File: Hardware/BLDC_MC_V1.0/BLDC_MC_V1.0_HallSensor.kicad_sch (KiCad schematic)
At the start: 21 parts, among them J5 Conn_02x03_Counter_Clockwise, U10 TLV9061IDBVR, U11 TLV9061IDBVR, U3 TLV9061IDBVR

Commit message: Add voltage sensor to measure the 3 phase voltage of inverter bridge
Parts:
- R15, R49, R52: LCSC_PN C98220 -> C95204; MP RC0603FR-0710KL -> RT0603BRD0710KL
- R46, R48, R51: LCSC_PN C100001 -> C723585; MP RC0603FR-0730KL -> RT0603BRD0730KL

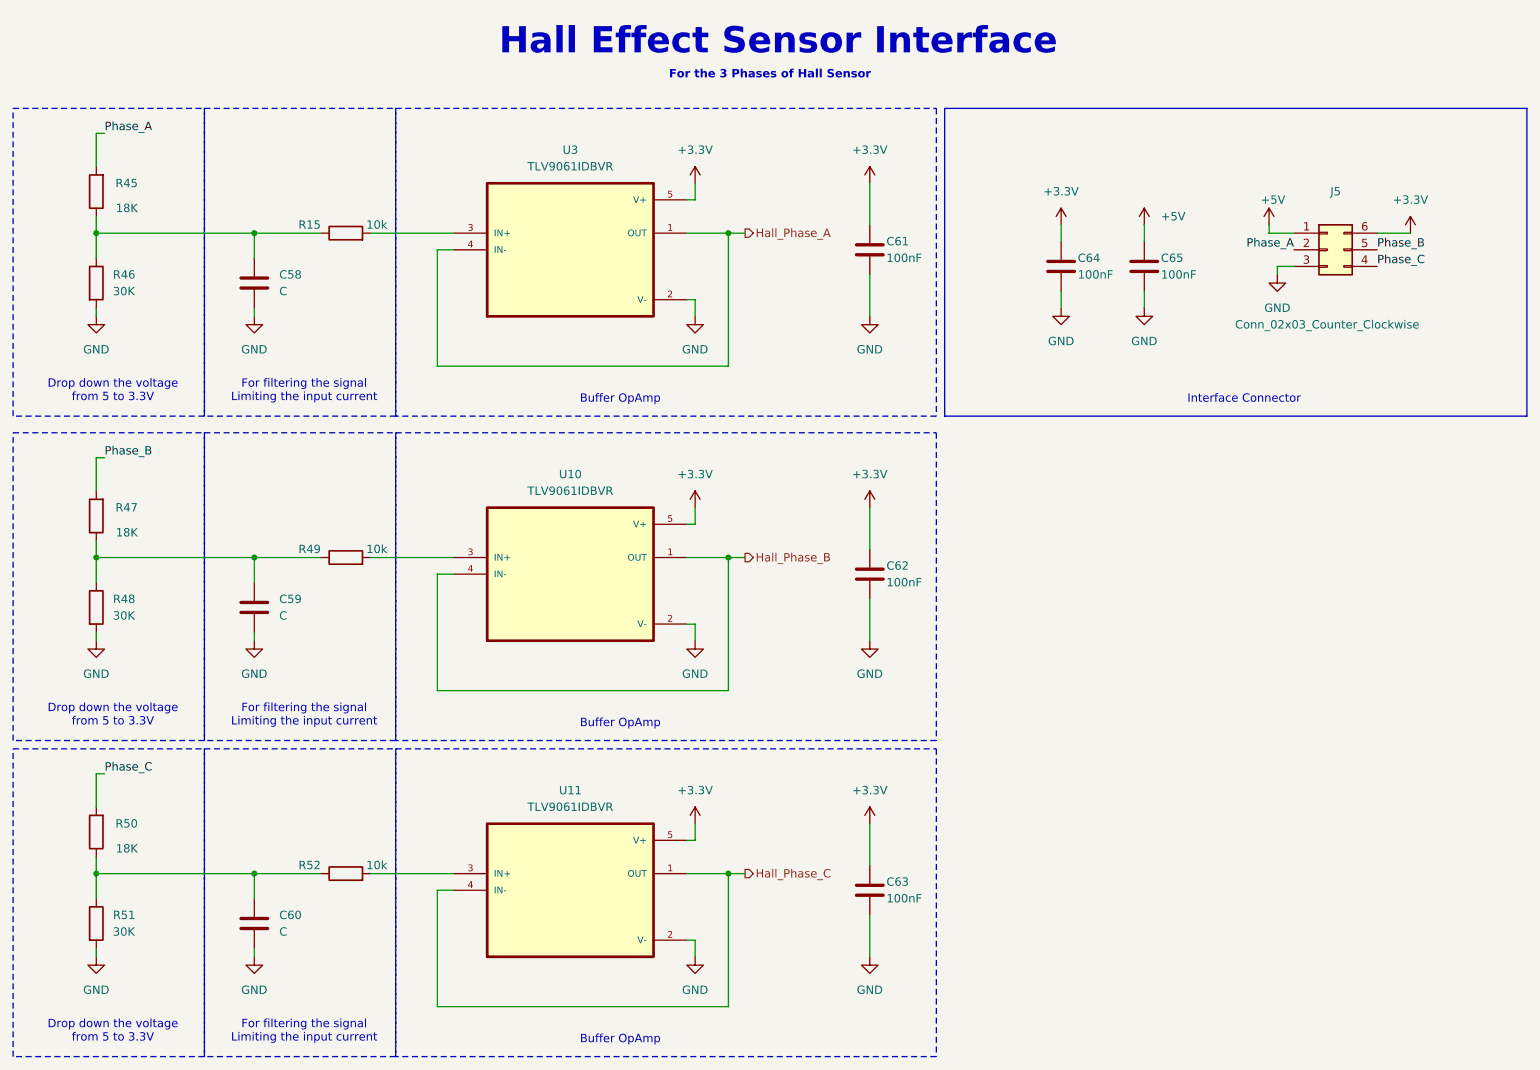
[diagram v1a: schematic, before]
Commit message: Add bypass capacitors for the OpAmps
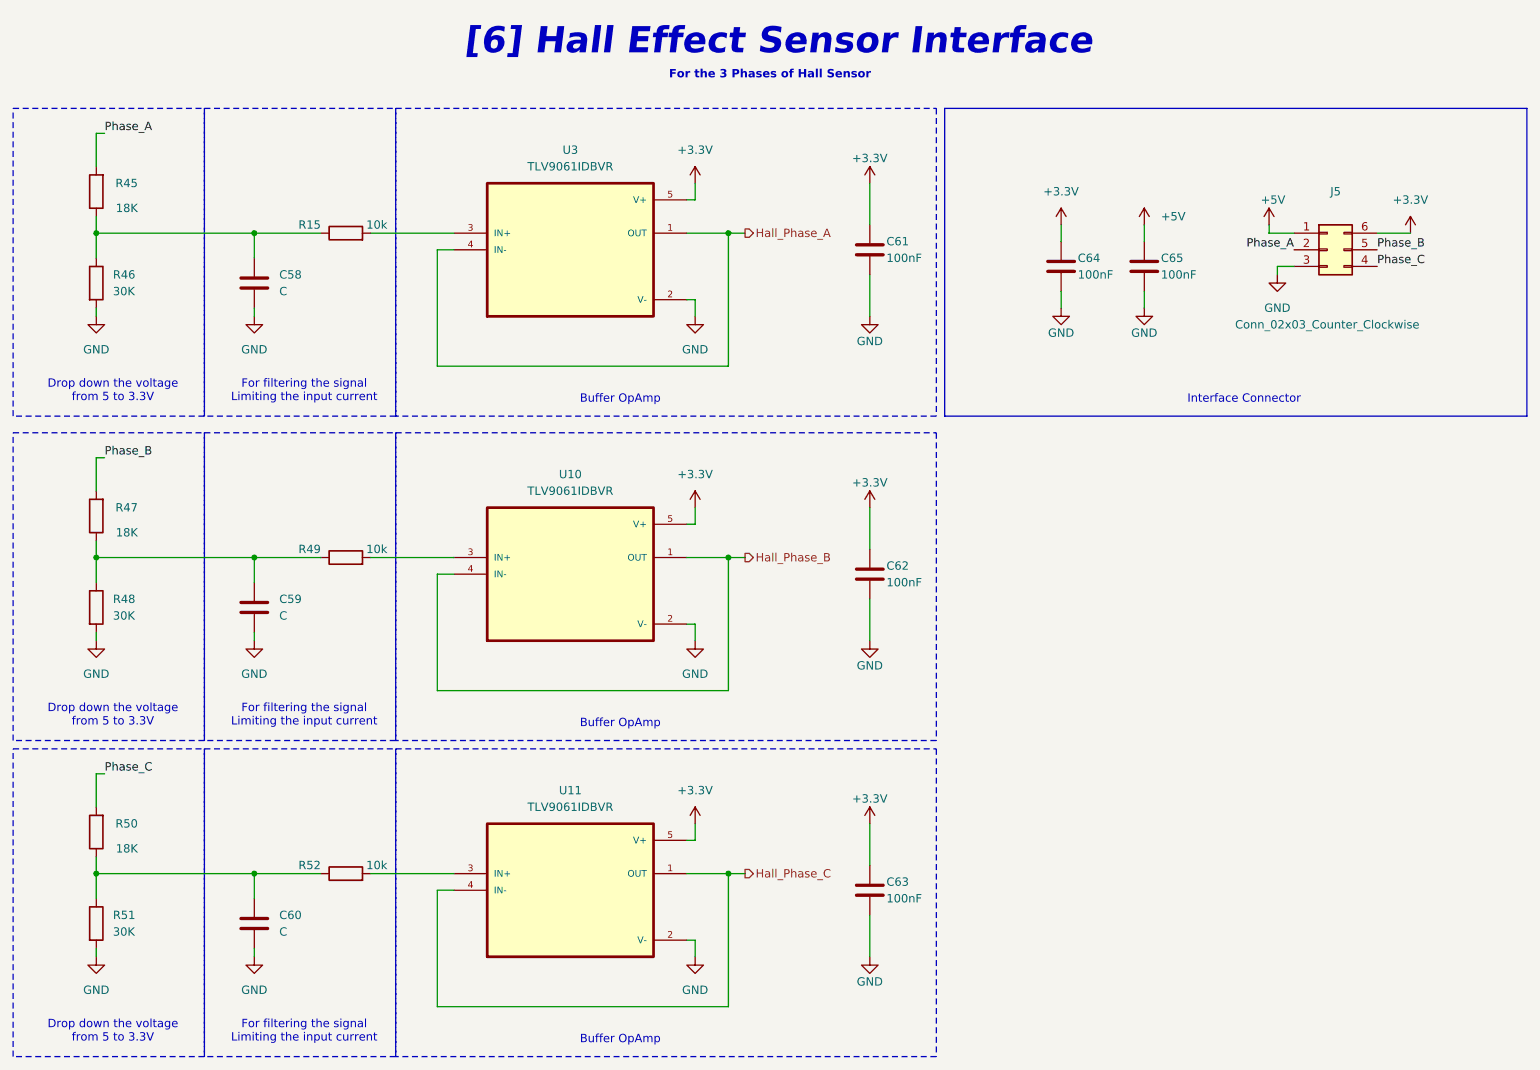
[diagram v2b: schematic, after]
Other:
- note added: "[6] Hall Effect Sensor Interface"
- note removed: "Hall Effect Sensor Interface"
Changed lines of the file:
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@@
 		)
 	)
-	(text "Hall Effect Sensor Interface"
+	(text "[6] Hall Effect Sensor Interface"
 		(exclude_from_sim no)
 		(at 142.24 26.67 0)
@@
 				(thickness 0.8)
 				(bold yes)
+				(italic yes)
 				(color 132 0 0 1)
 			)
@@
 		(on_board yes)
 		(dnp no)
-		(fields_autoplaced yes)
 		(property "Reference" "#PWR0113"
 			(at 185.42 73.66 0)
@@
 		)
 		(property "Value" "GND"
-			(at 185.42 72.39 0)
+			(at 185.42 71.12 0)
 			(effects
 				(font
@@
 		(on_board yes)
 		(dnp no)
-		(fields_autoplaced yes)
 		(property "Reference" "#PWR0111"
 			(at 156.21 172.72 0)
@@
 		)
 		(property "Value" "GND"
-			(at 156.21 171.45 0)
+			(at 156.21 170.18 0)
 			(effects
 				(font
@@
 		(on_board yes)
 		(dnp no)
-		(fields_autoplaced yes)
 		(property "Reference" "#PWR0107"
 			(at 156.21 74.93 0)
@@
 		)
 		(property "Value" "GND"
-			(at 156.21 73.66 0)
+			(at 156.21 72.39 0)
 			(effects
 				(font
@@
 		(on_board yes)
 		(dnp no)
-		(fields_autoplaced yes)
 		(property "Reference" "#PWR0108"
 			(at 156.21 101.6 0)
@@
 		)
 		(property "Value" "+3.3V"
-			(at 156.21 92.71 0)
+			(at 156.21 93.98 0)
 			(effects
 				(font
@@
 		(on_board yes)
 		(dnp no)
-		(fields_autoplaced yes)
 		(property "Reference" "#PWR0109"
 			(at 156.21 124.46 0)
@@
 		)
 		(property "Value" "GND"
-			(at 156.21 123.19 0)
+			(at 156.21 121.92 0)
 			(effects
 				(font
@@
 		(on_board yes)
 		(dnp no)
-		(fields_autoplaced yes)
 		(property "Reference" "#PWR0106"
 			(at 156.21 52.07 0)
@@
 		)
 		(property "Value" "+3.3V"
-			(at 156.21 43.18 0)
+			(at 156.21 44.45 0)
 			(effects
 				(font
@@
 		(on_board yes)
 		(dnp no)
-		(fields_autoplaced yes)
 		(property "Reference" "#PWR0110"
 			(at 156.21 149.86 0)
@@
 		)
 		(property "Value" "+3.3V"
-			(at 156.21 140.97 0)
+			(at 156.21 142.24 0)
 			(effects
 				(font
@@
 		(on_board yes)
 		(dnp no)
-		(fields_autoplaced yes)
 		(property "Reference" "#PWR0115"
 			(at 198.12 73.66 0)
@@
 		)
 		(property "Value" "GND"
-			(at 198.12 72.39 0)
+			(at 198.12 71.12 0)
 			(effects
 				(font

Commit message: Adjust the connections between sheets
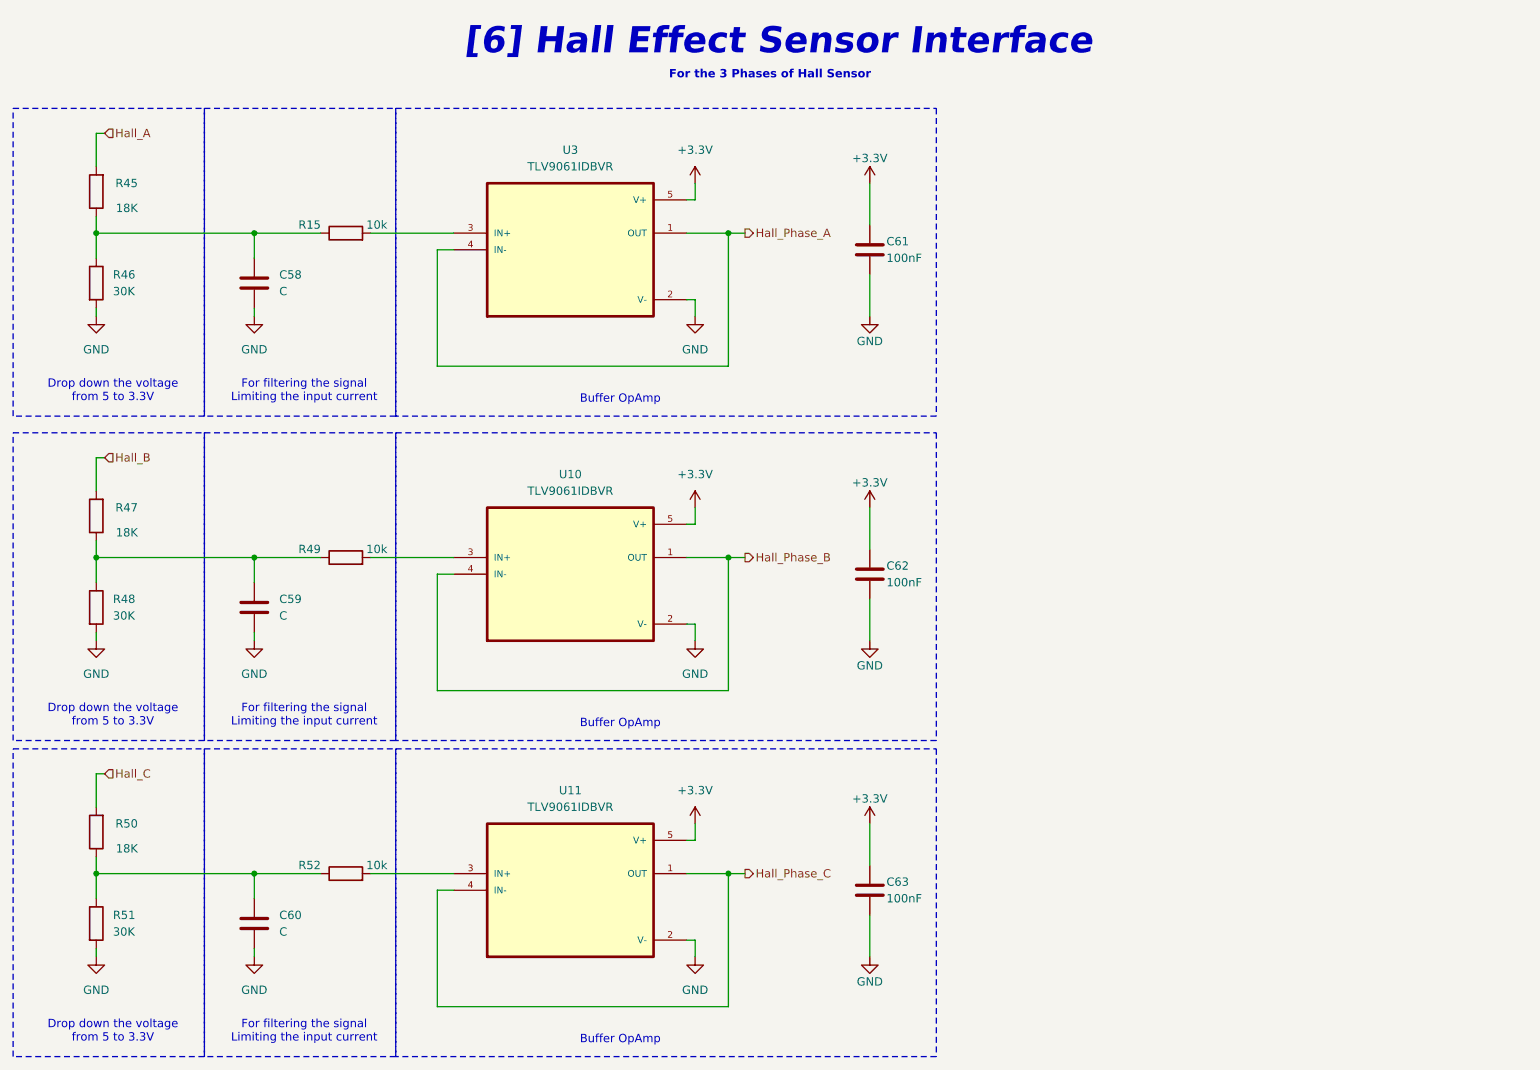
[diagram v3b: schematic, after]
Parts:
- removed C64, C65: 100nF, Capacitor_SMD:C_0805_2012Metric, symbol Device:C
- removed J5: Conn_02x03_Counter_Clockwise, Connector_Molex:Molex_Micro-Fit_3.0_43045-0612_2x03_P3.00mm_Vertical, symbol Connector_Generic:Conn_02x03_Counter_Clockwise
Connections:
- net Phase_A renamed Hall_A
- net Phase_B renamed Hall_B
- net Phase_C renamed Hall_C
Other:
- note removed: "Interface Connector"

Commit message: Solve all errors and wornings in project
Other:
- title: BLDC_MC_V1.0_HallSensor -> ${Project_Name}
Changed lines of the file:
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@@
 	(paper "A4")
 	(title_block
-		(title "BLDC_MC_V1.0_HallSensor")
+		(title "${Project_Name}")
 		(date "2026-03-05")
 		(rev "V1")
@@
 		(stroke
 			(width 0)
-			(type dash)
+			(type solid)
 		)
 		(fill
@@
 		(stroke
 			(width 0)
-			(type dash)
+			(type solid)
 		)
 		(fill
@@
 		(stroke
 			(width 0)
-			(type dash)
+			(type solid)
 		)
 		(fill
@@
 		(stroke
 			(width 0)
-			(type dash)
+			(type solid)
 		)
 		(fill
@@
 		(stroke
 			(width 0)
-			(type dash)
+			(type solid)
 		)
 		(fill
@@
 		(stroke
 			(width 0)
-			(type dash)
+			(type solid)
 		)
 		(fill
@@
 		(stroke
 			(width 0)
-			(type dash)
+			(type solid)
 		)
 		(fill
@@
 		(stroke
 			(width 0)
-			(type dash)
+			(type solid)
 		)
 		(fill
@@
 		(stroke
 			(width 0)
-			(type dash)
+			(type solid)
 		)
 		(fill
@@
 			)
 		)
-		(property "Datasheet" "https://www.lcsc.com/datasheet/C28233.pdf"
+		(property "Datasheet" "~"
 			(at 156.21 58.42 0)
 			(effects
@@
 			)
 		)
-		(property "Datasheet" "https://www.lcsc.com/datasheet/C95204.pdf"
+		(property "Datasheet" "~"
 			(at 76.2 55.88 0)
 			(effects
@@
 			)
 		)
-		(property "Datasheet" "https://www.lcsc.com/datasheet/C2906974.pdf"
+		(property "Datasheet" "~"
 			(at 38.1 49.53 0)
 			(effects
@@
 			)
 		)
-		(property "Datasheet" "https://www.lcsc.com/datasheet/C28233.pdf"
+		(property "Datasheet" "~"
 			(at 156.21 156.21 0)
 			(effects
@@
 			)
 		)
-		(property "Datasheet" "https://www.lcsc.com/datasheet/C2906974.pdf"
+		(property "Datasheet" "~"
 			(at 38.1 99.06 0)
 			(effects
@@
 			)
 		)
-		(property "Datasheet" "https://www.lcsc.com/datasheet/C95204.pdf"
+		(property "Datasheet" "~"
 			(at 76.2 153.67 0)
 			(effects
@@
 			)
 		)
-		(property "Datasheet" "https://www.lcsc.com/datasheet/C28233.pdf"
+		(property "Datasheet" "~"
 			(at 156.21 107.95 0)
 			(effects
@@
 			)
 		)
-		(property "Datasheet" "https://www.lcsc.com/datasheet/C723585.pdf"
+		(property "Datasheet" "~"
 			(at 38.1 63.5 0)
 			(effects
@@
 			)
 		)
-		(property "Datasheet" "https://www.lcsc.com/datasheet/C2906974.pdf"
+		(property "Datasheet" "~"
 			(at 38.1 147.32 0)
 			(effects
@@
 			)
 		)
-		(property "Datasheet" "https://www.lcsc.com/datasheet/C95204.pdf"
+		(property "Datasheet" "~"
 			(at 76.2 105.41 0)
 			(effects
@@
 			)
 		)
-		(property "Datasheet" "https://www.lcsc.com/datasheet/C723585.pdf"
+		(property "Datasheet" "~"
 			(at 38.1 113.03 0)
 			(effects
@@
 			)
 		)
-		(property "Datasheet" "https://www.lcsc.com/datasheet/C723585.pdf"
+		(property "Datasheet" "~"
 			(at 38.1 161.29 0)
 			(effects

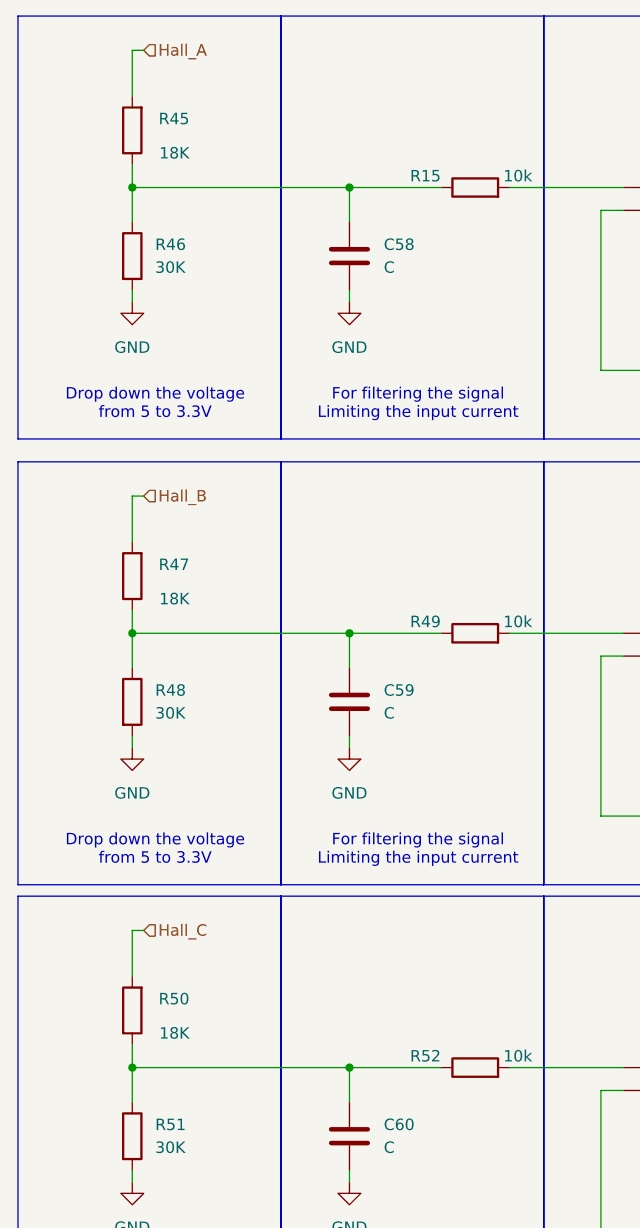
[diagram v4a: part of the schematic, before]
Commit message: Run DRC and solve all errors and warnings (project updated to Kicad 10)
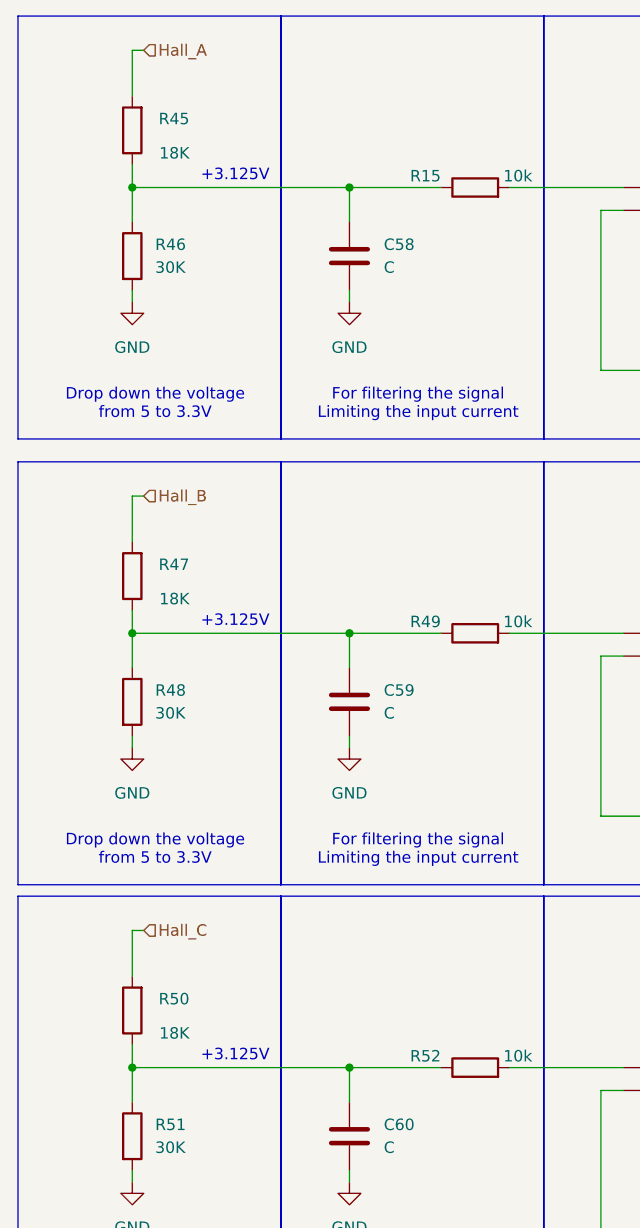
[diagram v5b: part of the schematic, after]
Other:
- note added: "+3.125V"
